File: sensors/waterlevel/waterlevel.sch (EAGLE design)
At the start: 87 parts, among them IC2 MCP604SL, IC3 MCP601SN, IC4 MCP601SN, P1 CAMDEN-CTB5000/6, P2 CTB1500/2, U1 NCP1729SN35T1G, U2 SR05S05, U3 VISHAY-VCUT05A4, U4 VISHAY-VCUT05A4, U5 LP3981IMM-3.3

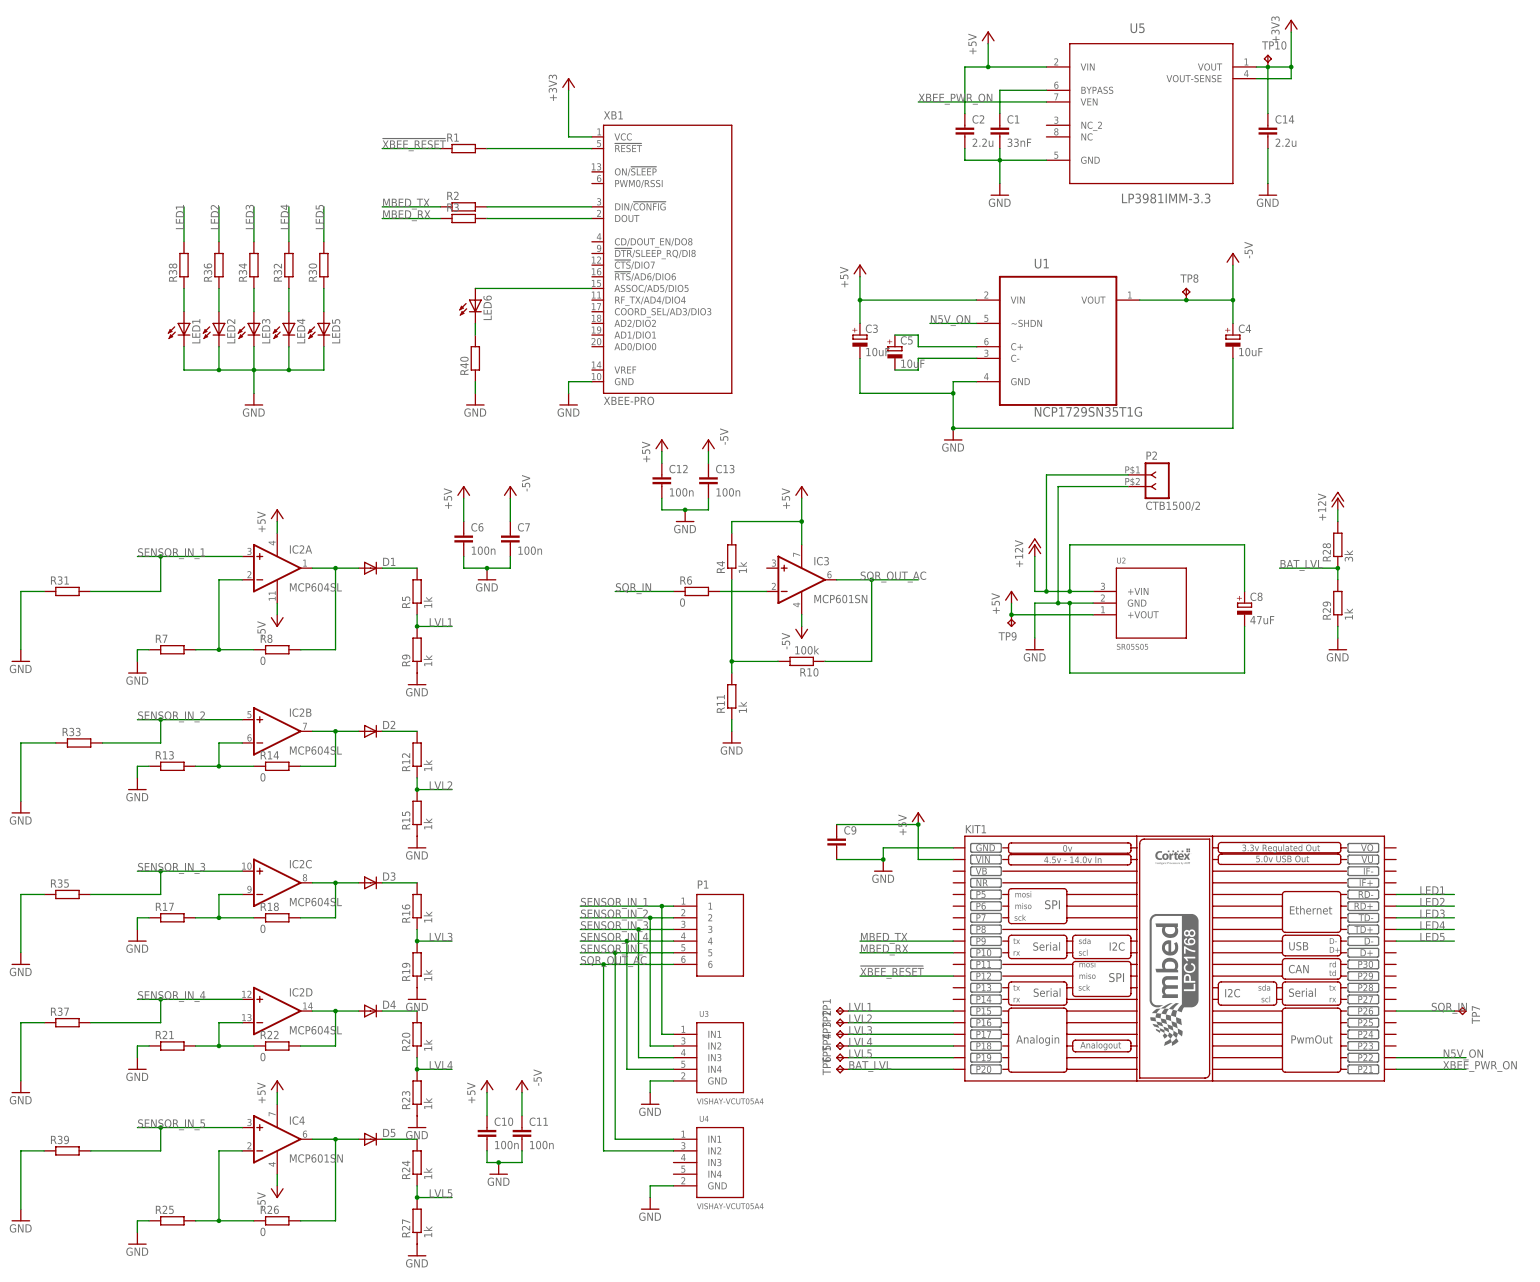
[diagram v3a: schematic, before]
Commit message: [WSensor] Fixed bug with unconnected opamp input. Fixed component values.
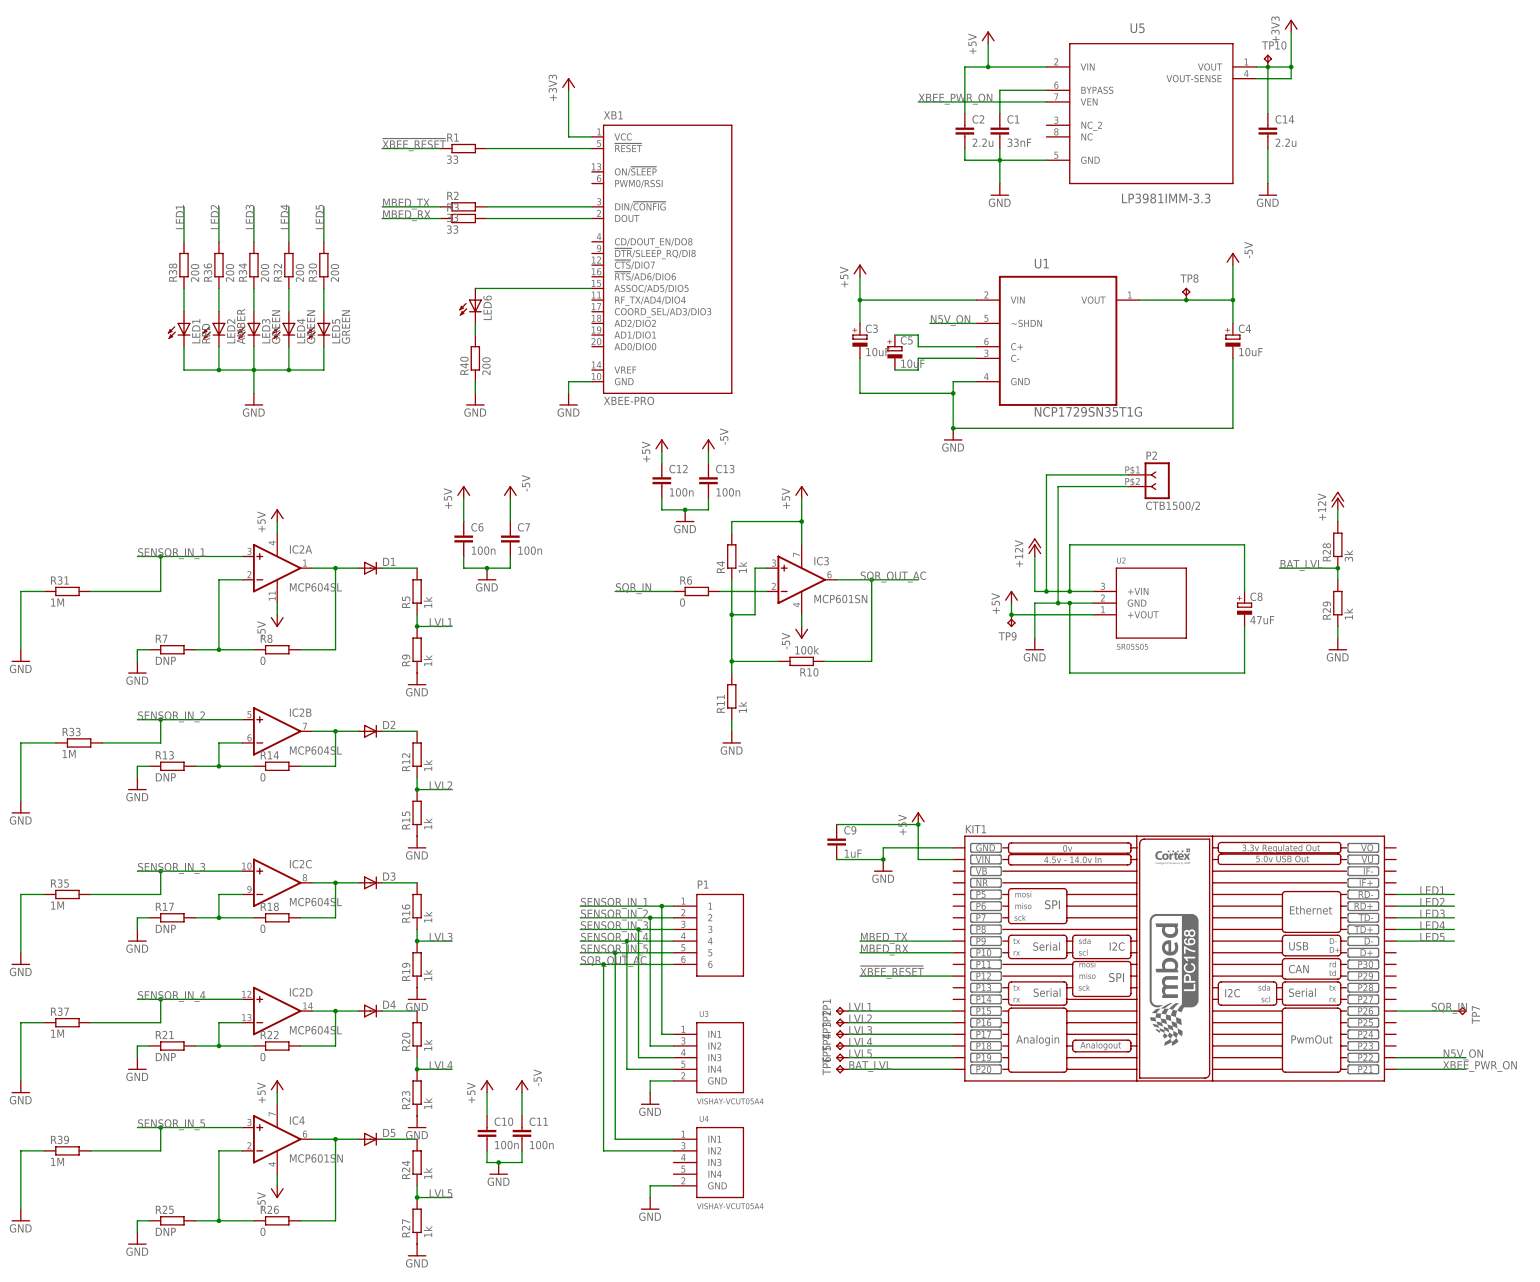
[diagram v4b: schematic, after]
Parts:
- C9: value (none) -> 1uF
- LED1: value (none) -> RED
- LED2: value (none) -> AMBER
- LED3, LED4, LED5: value (none) -> GREEN
- R1, R2, R3: value (none) -> 33
- R13, R17, R21, R25, R7: value (none) -> DNP
- R30, R32, R34, R36, R38, R40: value (none) -> 200
- R31, R33, R35, R37, R39: value (none) -> 1M
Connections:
- net N$23: now also IC3.+IN
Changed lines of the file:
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@@
 <part name="R26" library="resistor" deviceset="R-EU_" device="R0603" value="0"/>
 <part name="R8" library="resistor" deviceset="R-EU_" device="R0603" value="0"/>
-<part name="R21" library="resistor" deviceset="R-EU_" device="R0603"/>
-<part name="R25" library="resistor" deviceset="R-EU_" device="R0603"/>
-<part name="R17" library="resistor" deviceset="R-EU_" device="R0603"/>
-<part name="R13" library="resistor" deviceset="R-EU_" device="R0603"/>
-<part name="R7" library="resistor" deviceset="R-EU_" device="R0603"/>
+<part name="R21" library="resistor" deviceset="R-EU_" device="R0603" value="DNP"/>
+<part name="R25" library="resistor" deviceset="R-EU_" device="R0603" value="DNP"/>
+<part name="R17" library="resistor" deviceset="R-EU_" device="R0603" value="DNP"/>
+<part name="R13" library="resistor" deviceset="R-EU_" device="R0603" value="DNP"/>
+<part name="R7" library="resistor" deviceset="R-EU_" device="R0603" value="DNP"/>
 <part name="GND1" library="supply1" deviceset="GND" device=""/>
 <part name="GND2" library="supply1" deviceset="GND" device=""/>
@@
 <part name="C10" library="resistor" deviceset="C-EU" device="C1206" value="100n"/>
 <part name="C11" library="resistor" deviceset="C-EU" device="C1206" value="100n"/>
-<part name="C9" library="resistor" deviceset="C-EU" device="C1206"/>
+<part name="C9" library="resistor" deviceset="C-EU" device="C1206" value="1uF"/>
 <part name="GND15" library="supply1" deviceset="GND" device=""/>
 <part name="GND16" library="supply1" deviceset="GND" device=""/>
@@
 <part name="GND20" library="supply1" deviceset="GND" device=""/>
 <part name="+3V2" library="supply1" deviceset="+3V3" device=""/>
-<part name="R1" library="resistor" deviceset="R-EU_" device="R0603"/>
-<part name="R2" library="resistor" deviceset="R-EU_" device="R0603"/>
-<part name="R3" library="resistor" deviceset="R-EU_" device="R0603"/>
+<part name="R1" library="resistor" deviceset="R-EU_" device="R0603" value="33"/>
+<part name="R2" library="resistor" deviceset="R-EU_" device="R0603" value="33"/>
+<part name="R3" library="resistor" deviceset="R-EU_" device="R0603" value="33"/>
 <part name="P2" library="eko-parts" deviceset="CTB1500/2" device=""/>
 <part name="C12" library="resistor" deviceset="C-EU" device="C1206" value="100n"/>
@@
 <part name="R28" library="resistor" deviceset="R-EU_" device="R0805" value="3k"/>
 <part name="R29" library="resistor" deviceset="R-EU_" device="R0805" value="1k"/>
-<part name="R31" library="resistor" deviceset="R-EU_" device="R0805"/>
+<part name="R31" library="resistor" deviceset="R-EU_" device="R0805" value="1M"/>
 <part name="GND24" library="supply1" deviceset="GND" device=""/>
-<part name="R33" library="resistor" deviceset="R-EU_" device="R0805"/>
+<part name="R33" library="resistor" deviceset="R-EU_" device="R0805" value="1M"/>
 <part name="GND25" library="supply1" deviceset="GND" device=""/>
-<part name="R35" library="resistor" deviceset="R-EU_" device="R0805"/>
+<part name="R35" library="resistor" deviceset="R-EU_" device="R0805" value="1M"/>
 <part name="GND26" library="supply1" deviceset="GND" device=""/>
-<part name="R37" library="resistor" deviceset="R-EU_" device="R0805"/>
+<part name="R37" library="resistor" deviceset="R-EU_" device="R0805" value="1M"/>
 <part name="GND27" library="supply1" deviceset="GND" device=""/>
-<part name="R39" library="resistor" deviceset="R-EU_" device="R0805"/>
+<part name="R39" library="resistor" deviceset="R-EU_" device="R0805" value="1M"/>
 <part name="GND28" library="supply1" deviceset="GND" device=""/>
-<part name="LED1" library="led" deviceset="LED" device="CHIPLED_0805"/>
-<part name="LED2" library="led" deviceset="LED" device="CHIPLED_0805"/>
-<part name="LED3" library="led" deviceset="LED" device="CHIPLED_0805"/>
-<part name="LED4" library="led" deviceset="LED" device="CHIPLED_0805"/>
-<part name="LED5" library="led" deviceset="LED" device="CHIPLED_0805"/>
+<part name="LED1" library="led" deviceset="LED" device="CHIPLED_0805" value="RED"/>
+<part name="LED2" library="led" deviceset="LED" device="CHIPLED_0805" value="AMBER"/>
+<part name="LED3" library="led" deviceset="LED" device="CHIPLED_0805" value="GREEN"/>
+<part name="LED4" library="led" deviceset="LED" device="CHIPLED_0805" value="GREEN"/>
+<part name="LED5" library="led" deviceset="LED" device="CHIPLED_0805" value="GREEN"/>
 <part name="LED6" library="led" deviceset="LED" device="CHIPLED_0805"/>
-<part name="R30" library="resistor" deviceset="R-EU_" device="R0603"/>
-<part name="R32" library="resistor" deviceset="R-EU_" device="R0603"/>
-<part name="R34" library="resistor" deviceset="R-EU_" device="R0603"/>
-<part name="R36" library="resistor" deviceset="R-EU_" device="R0603"/>
-<part name="R38" library="resistor" deviceset="R-EU_" device="R0603"/>
-<part name="R40" library="resistor" deviceset="R-EU_" device="R0603"/>
+<part name="R30" library="resistor" deviceset="R-EU_" device="R0603" value="200"/>
+<part name="R32" library="resistor" deviceset="R-EU_" device="R0603" value="200"/>
+<part name="R34" library="resistor" deviceset="R-EU_" device="R0603" value="200"/>
+<part name="R36" library="resistor" deviceset="R-EU_" device="R0603" value="200"/>
+<part name="R38" library="resistor" deviceset="R-EU_" device="R0603" value="200"/>
+<part name="R40" library="resistor" deviceset="R-EU_" device="R0603" value="200"/>
 <part name="GND29" library="supply1" deviceset="GND" device=""/>
 <part name="GND30" library="supply1" deviceset="GND" device=""/>
@@
 <pinref part="R4" gate="G$1" pin="1"/>
 <pinref part="R11" gate="G$1" pin="2"/>
-<wire x1="109.22" y1="147.32" x2="109.22" y2="129.54" width="0.1524" layer="91"/>
+<wire x1="109.22" y1="147.32" x2="109.22" y2="139.7" width="0.1524" layer="91"/>
+<wire x1="109.22" y1="139.7" x2="109.22" y2="129.54" width="0.1524" layer="91"/>
 <wire x1="109.22" y1="129.54" x2="109.22" y2="127" width="0.1524" layer="91"/>
 <junction x="109.22" y="129.54"/>
 <pinref part="R10" gate="G$1" pin="2"/>
 <wire x1="109.22" y1="129.54" x2="119.38" y2="129.54" width="0.1524" layer="91"/>
-</segment>
-</net>
+<pinref part="IC3" gate="G$1" pin="+IN"/>
+<wire x1="116.84" y1="149.86" x2="114.3" y2="149.86" width="0.1524" layer="91"/>
+<wire x1="114.3" y1="149.86" x2="114.3" y2="139.7" width="0.1524" layer="91"/>
+<wire x1="114.3" y1="139.7" x2="109.22" y2="139.7" width="0.1524" layer="91"/>
+<junction x="109.22" y="139.7"/>
+</segment>
+</net>
